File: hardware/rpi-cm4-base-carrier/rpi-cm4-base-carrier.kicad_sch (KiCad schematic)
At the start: 0 parts

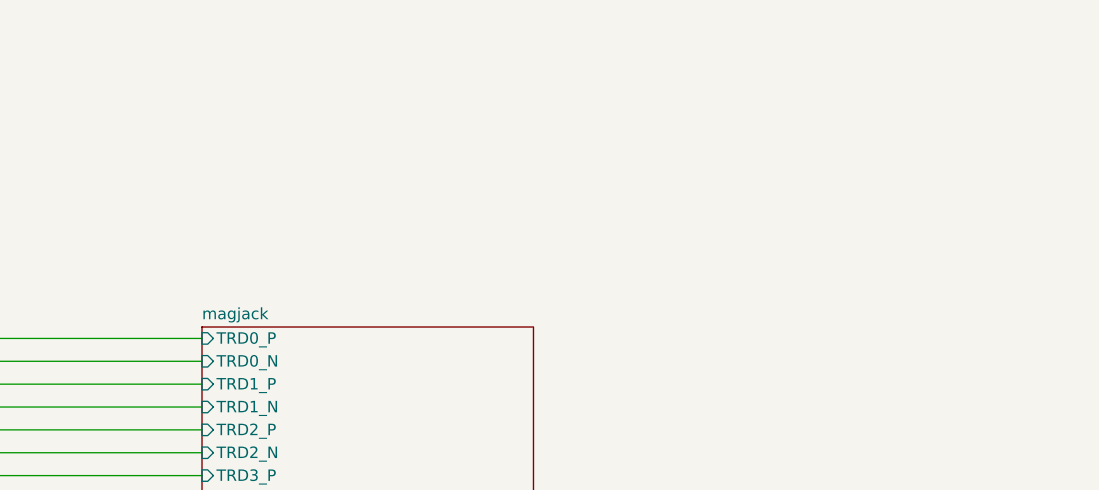
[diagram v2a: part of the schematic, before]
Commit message: fan control added to sch, layout 90% complete, awaiting review
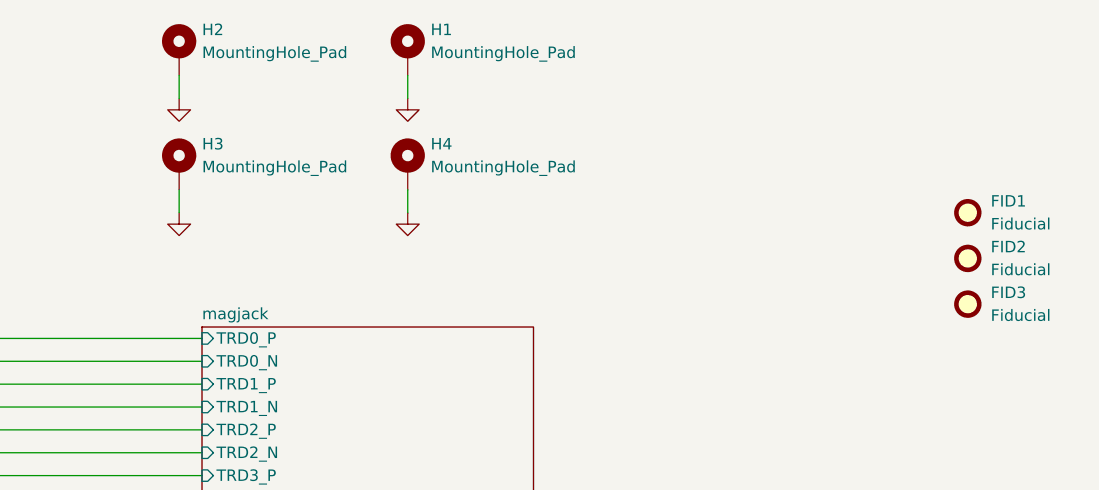
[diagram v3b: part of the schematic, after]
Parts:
- added FID1, FID2, FID3: Fiducial, Fiducial:Fiducial_1.5mm_Mask3mm, symbol Mechanical:Fiducial
- added H1, H2, H3, H4: MountingHole_Pad, MountingHole:MountingHole_4.3mm_M4_DIN965_Pad_TopBottom, symbol Mechanical:MountingHole_Pad
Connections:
- new net GND: H1.1, H2.1, H3.1, H4.1

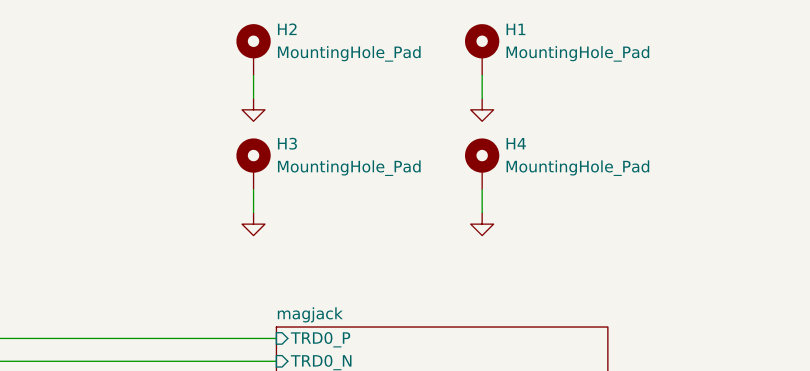
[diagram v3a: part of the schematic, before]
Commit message: convert IC refs to U refs and re-annotate, add fiducials and extra via stitching to layout
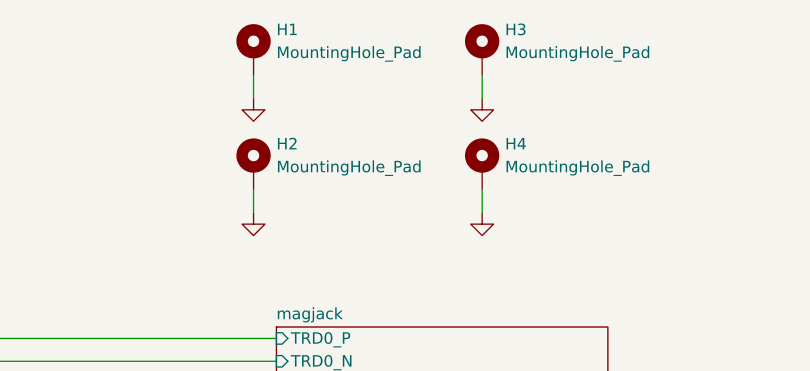
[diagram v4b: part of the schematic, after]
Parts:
- renumbered H2 to H1, H3 to H2, H1 to H3

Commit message: design files exported ready for manufacture, LCSC part numbers added throughout the library
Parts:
- FID1, FID2, FID3, H1, H2, H3, H4: LCSC Part # (none) -> NF; LCSC Part Number (none) -> NF
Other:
- title: Raspberry Pi Compute Module 4 Base Carrier -> Raspberry Pi Compute Module 4 Control Node
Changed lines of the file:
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@@
   (paper "A4")
   (title_block
-    (title "Raspberry Pi Compute Module 4 Base Carrier")
-    (date "2020-10-31")
+    (title "Raspberry Pi Compute Module 4 Control Node")
+    (date "2024-02-04")
     (rev "v01")
     (comment 2 "creativecommons.org/licenses/by-sa/4.0/")
     (comment 3 "License: CC BY-SA 4.0")
-    (comment 4 "Author: Shawn Hymel")
+    (comment 4 "Author: Sam Earnshaw")
   )
   (junction (at 92.71 54.61) (diameter 0) (color 0 0 0 0)
@@
       (effects (font (size 1.27 1.27)) hide)
     )
+    (property "LCSC Part Number" "NF" (at 200.66 33.02 0)
+      (effects (font (size 1.27 1.27)) hide)
+    )
+    (property "LCSC Part #" "NF" (at 200.66 33.02 0)
+      (effects (font (size 1.27 1.27)) hide)
+    )
     (pin "1")
     (instances
@@
       (effects (font (size 1.27 1.27)) hide)
     )
+    (property "LCSC Part Number" "NF" (at 175.26 33.02 0)
+      (effects (font (size 1.27 1.27)) hide)
+    )
+    (property "LCSC Part #" "NF" (at 175.26 33.02 0)
+      (effects (font (size 1.27 1.27)) hide)
+    )
     (pin "1")
     (instances
@@
     )
     (property "Datasheet" "~" (at 175.26 20.32 0)
+      (effects (font (size 1.27 1.27)) hide)
+    )
+    (property "LCSC Part Number" "NF" (at 175.26 20.32 0)
+      (effects (font (size 1.27 1.27)) hide)
+    )
+    (property "LCSC Part #" "NF" (at 175.26 20.32 0)
       (effects (font (size 1.27 1.27)) hide)
     )
@@
       (effects (font (size 1.27 1.27)) hide)
     )
+    (property "LCSC Part Number" "NF" (at 262.89 48.26 0)
+      (effects (font (size 1.27 1.27)) hide)
+    )
+    (property "LCSC Part #" "NF" (at 262.89 48.26 0)
+      (effects (font (size 1.27 1.27)) hide)
+    )
     (instances
       (project "rpi-cm4-base-carrier"
@@
       (effects (font (size 1.27 1.27)) hide)
     )
+    (property "LCSC Part Number" "NF" (at 262.89 43.18 0)
+      (effects (font (size 1.27 1.27)) hide)
+    )
+    (property "LCSC Part #" "NF" (at 262.89 43.18 0)
+      (effects (font (size 1.27 1.27)) hide)
+    )
     (instances
       (project "rpi-cm4-base-carrier"
@@
     )
     (property "Datasheet" "~" (at 262.89 38.1 0)
+      (effects (font (size 1.27 1.27)) hide)
+    )
+    (property "LCSC Part Number" "NF" (at 262.89 38.1 0)
+      (effects (font (size 1.27 1.27)) hide)
+    )
+    (property "LCSC Part #" "NF" (at 262.89 38.1 0)
       (effects (font (size 1.27 1.27)) hide)
     )
@@
       (effects (font (size 1.27 1.27)) hide)
     )
+    (property "LCSC Part Number" "NF" (at 200.66 20.32 0)
+      (effects (font (size 1.27 1.27)) hide)
+    )
+    (property "LCSC Part #" "NF" (at 200.66 20.32 0)
+      (effects (font (size 1.27 1.27)) hide)
+    )
